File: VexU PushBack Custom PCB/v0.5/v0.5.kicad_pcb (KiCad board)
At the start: 2 copper layers, 47 parts, among them J1 Conn_01x04_Pin, J2 4P4C, J3 Conn_01x04_Pin, J4 USB_B_Micro, SW1 SW_SPDT, U1 STM32G431RBT6, U2 MP2338GTL-P, U3 MAX485E, Y1 16MHz

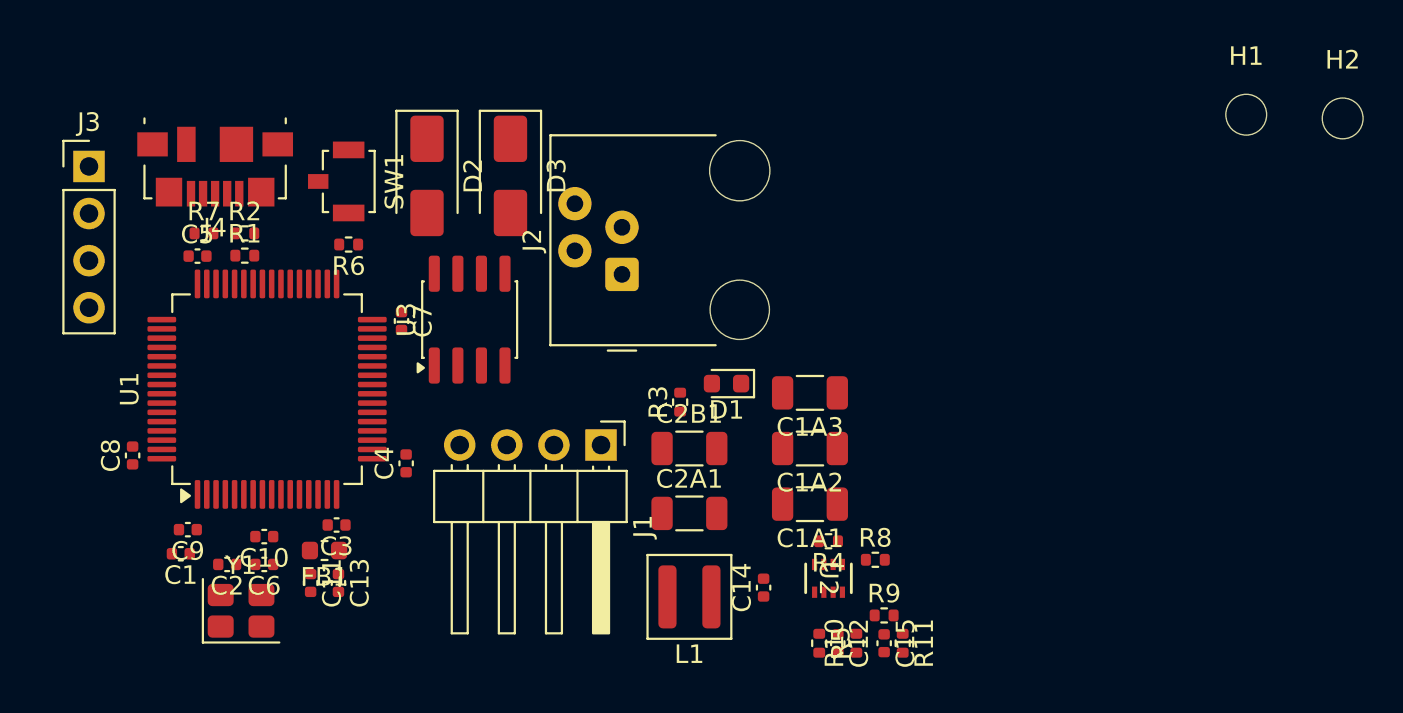
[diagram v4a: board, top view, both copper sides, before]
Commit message: Added SparkFun Library
Switched 1mm 1x4 connect out for QWIIC connector
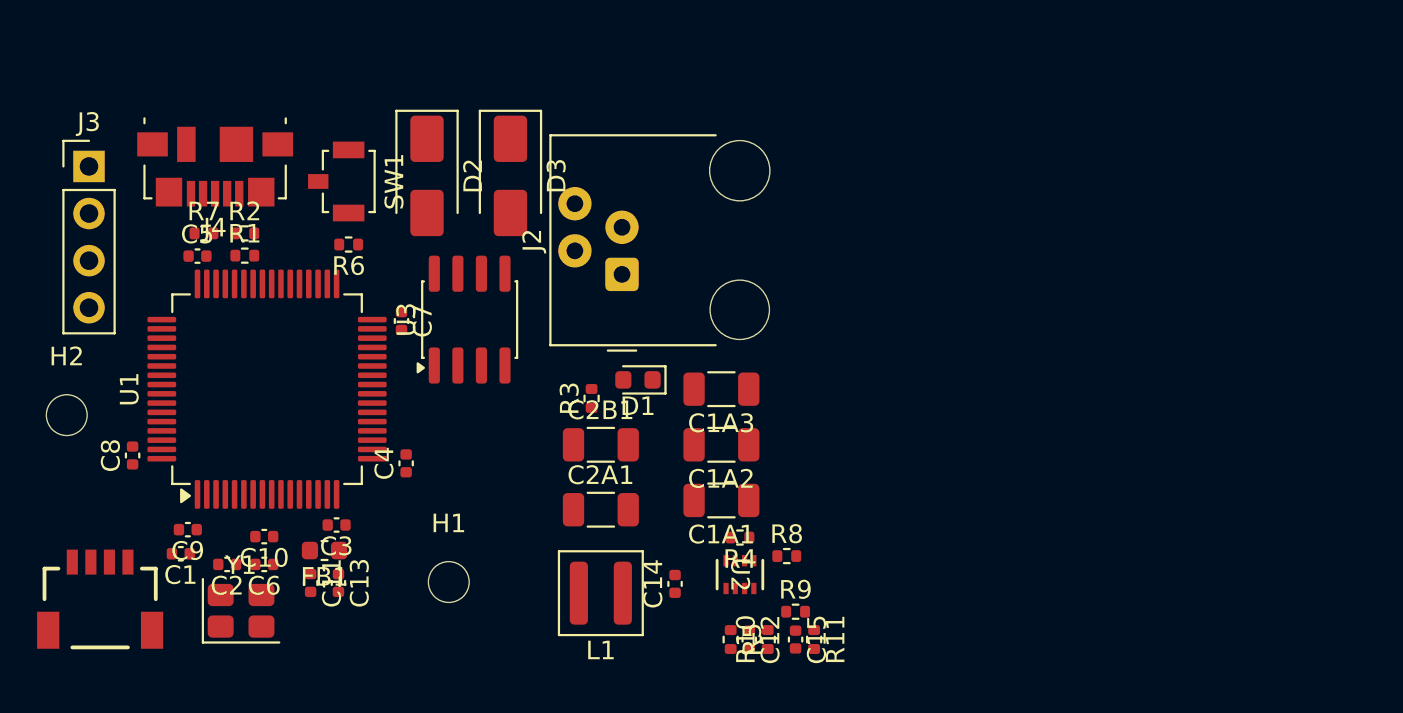
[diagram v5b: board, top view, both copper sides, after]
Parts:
- removed J1: Conn_01x04_Pin, Connector_PinHeader_2.54mm:PinHeader_1x04_P2.54mm_Horizontal
- added J5: Qwiic_RA, SparkFun-Connector:JST_1x04_P1.0mm_Horizontal_SMD, F.Cu at (79.2, 65.7)
- moved H2 70.6 mm to (77.4, 57.8)
- moved H1 49.8 mm to (98.0, 66.8)
- moved R8 4.78 mm to (116.2, 65.4)
- moved C1A1 4.78 mm to (112.7, 62.4)
- moved C1A2 4.78 mm to (112.7, 59.4)
- moved C1A3 4.78 mm to (112.7, 56.4)
- moved C2A1 4.78 mm to (106.2, 62.9)
- moved C2B1 4.78 mm to (106.2, 59.4)
- moved D1 4.78 mm to (108.2, 55.9)
- moved R3 4.78 mm to (105.7, 56.9)
- moved C12 4.78 mm to (114.2, 69.9)
- moved C14 4.78 mm to (110.2, 66.9)
- moved C15 4.78 mm to (116.7, 69.9)
- moved L1 4.78 mm to (106.2, 67.4)
- moved R10 4.78 mm to (115.2, 69.9)
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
